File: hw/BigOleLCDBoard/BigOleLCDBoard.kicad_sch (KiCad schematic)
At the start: 11 parts, among them J101 Conn_01x02, J102 Conn_01x04, J103 Conn_01x08, J104 Conn_01x08, U101 OD-103, U102 OD-103, U103 OD-103, U104 OD-103, U105 CY8CKIT-049-4XXX

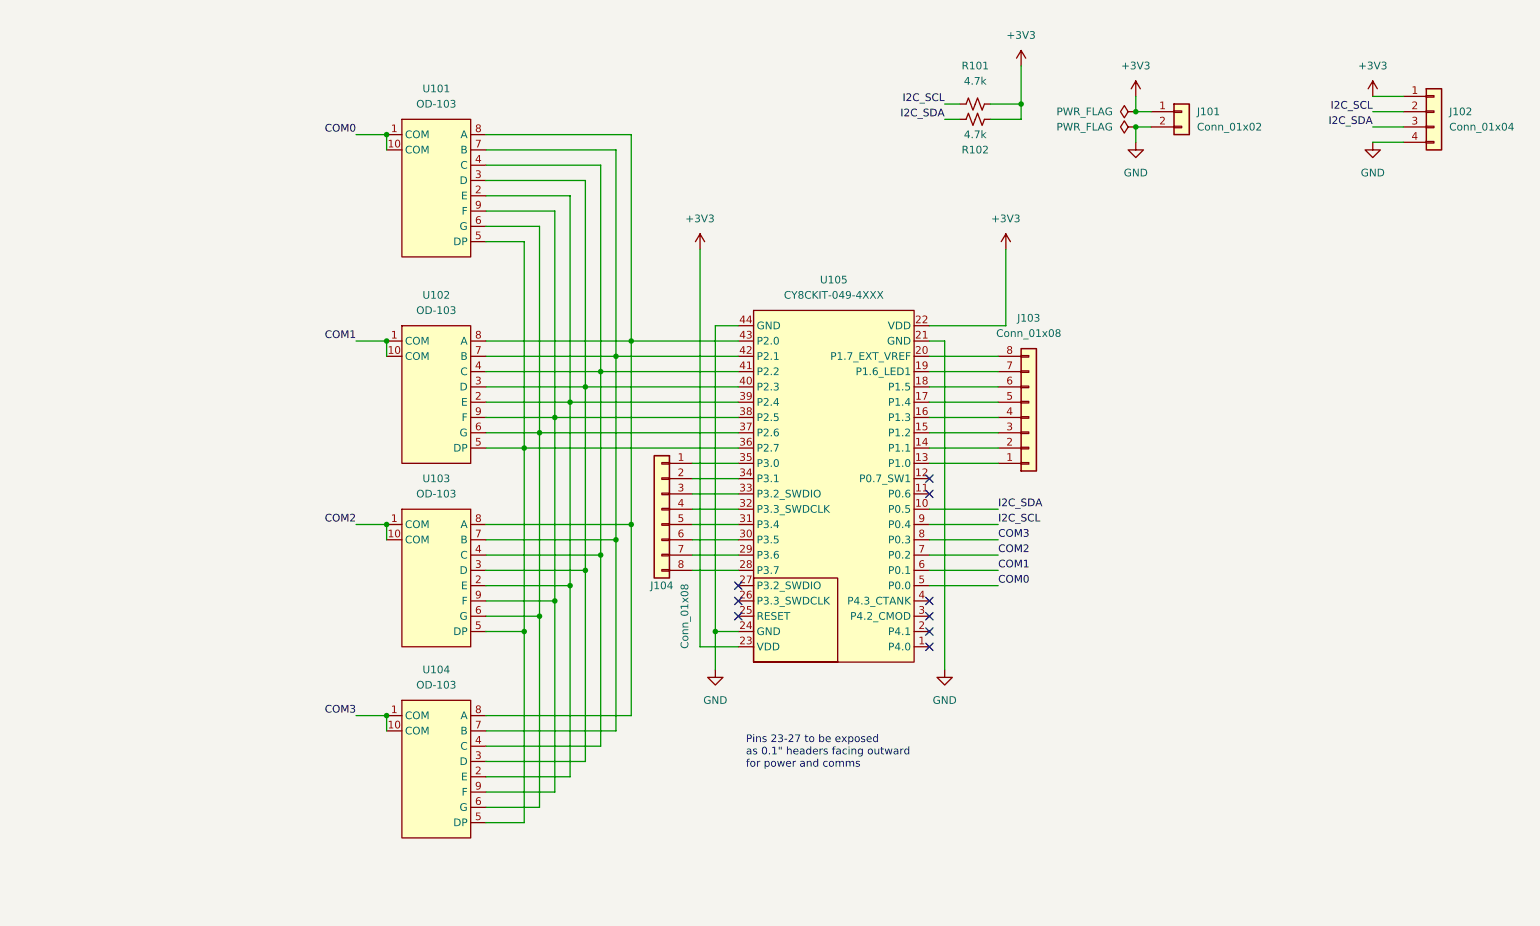
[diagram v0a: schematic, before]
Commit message: Ask WeMos D1-Mini, start layout
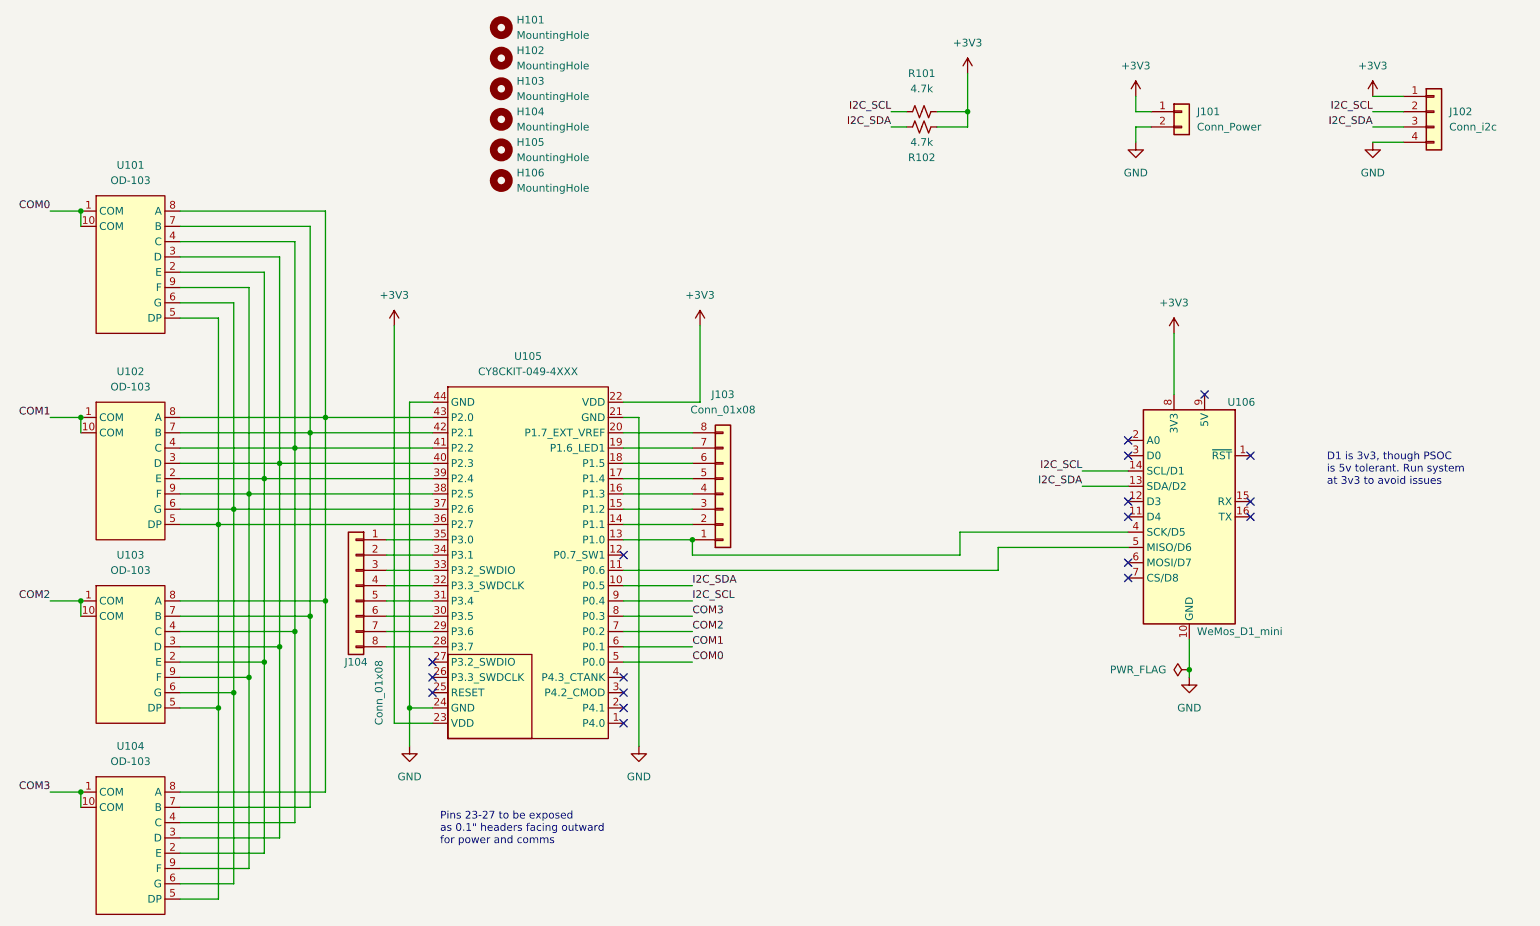
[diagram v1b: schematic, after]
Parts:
- added H101, H102, H103, H104, H105, H106: MountingHole, MountingHole:MountingHole_4.3mm_M4, symbol Mechanical:MountingHole
- added U106: WeMos_D1_mini, Module:WEMOS_D1_mini_light, symbol MCU_Module:WeMos_D1_mini
- J101: value Conn_01x02 -> Conn_Power
- J102: value Conn_01x04 -> Conn_i2c
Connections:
- net +3V3: now also U106.8 (3V3)
- net GND: now also U106.10 (GND)
- net I2C_SCL: now also U106.14 (SCL/D1)
- net I2C_SDA: now also U106.13 (SDA/D2)
- net at U105.11 (P0.6): now also U106.5 (MISO/D6)
- net at J103.1 (Pin_1), U105.13 (P1.0): now also U106.4 (SCK/D5)
- no-connect marks 9 -> 18
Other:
- note added: "D1 is 3v3, though PSOC is 5v tolerant. Run system at 3v3 to avoid issues"
- moved on the sheet: J103, J104, R101, R102, U101, U102, U103, U104, U105
